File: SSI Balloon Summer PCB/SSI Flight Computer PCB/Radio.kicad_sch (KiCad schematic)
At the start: 5 parts, among them J3 LoRa antenna, U1 RFM95W-915S2

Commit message: Cleaned APRS Filter up and adding Testing points
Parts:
- added TP12, TP13, TP7: TestPoint, TestPoint:TestPoint_Pad_1.5x1.5mm, symbol Connector:TestPoint
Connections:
- net GND: now also TP13.1
- net LoRa_DIO0: now also TP12.1
- net LoRa_RESET: now also TP7.1

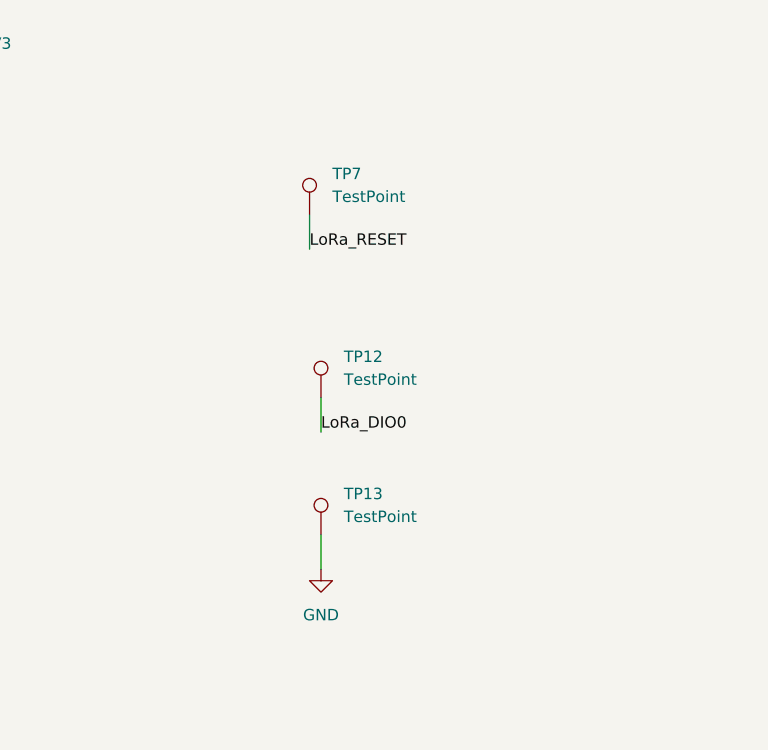
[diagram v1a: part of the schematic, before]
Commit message: Added Headers for testing, finalizing PCB
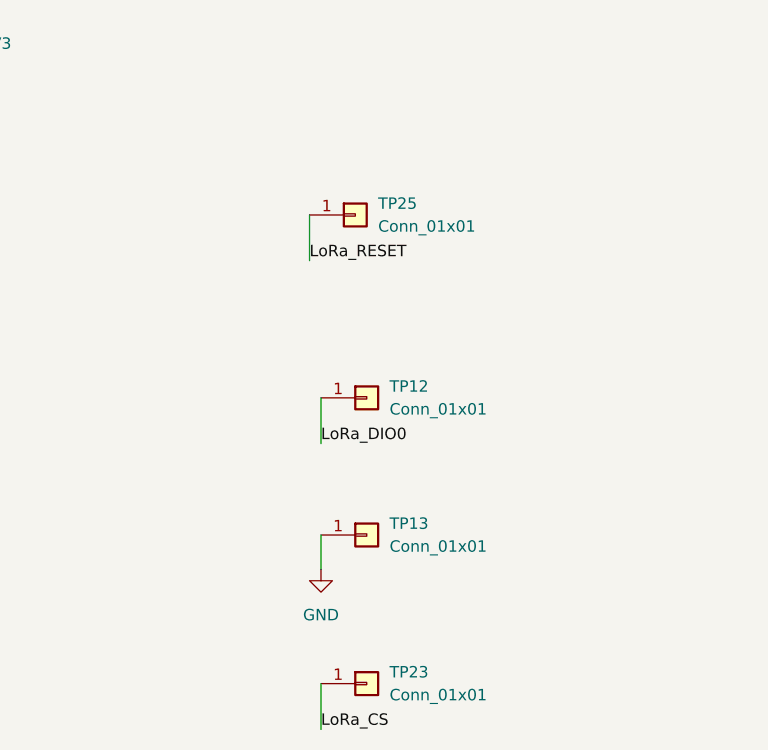
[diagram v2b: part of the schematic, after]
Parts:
- removed TP12, TP13, TP7: TestPoint, TestPoint:TestPoint_Pad_1.5x1.5mm, symbol Connector:TestPoint
- added TP12, TP13, TP23, TP25: Conn_01x01, Connector_PinHeader_2.54mm:PinHeader_1x01_P2.54mm_Vertical, symbol Connector_Generic:Conn_01x01
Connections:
- net GND: now also TP13.1 (Pin_1)
- net LoRa_CS: now also TP23.1 (Pin_1)
- net LoRa_DIO0: now also TP12.1 (Pin_1)
- net LoRa_RESET: now also TP25.1 (Pin_1)
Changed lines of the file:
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@@
+	(wire
+		(pts
+			(xy 231.14 139.7) (xy 231.14 144.78)
+		)
+		(stroke
+			(width 0)
+			(type default)
+		)
+	)
 	(wire
 		(pts
@@
 	(wire
 		(pts
-			(xy 229.87 87.63) (xy 229.87 91.44)
+			(xy 229.87 87.63) (xy 229.87 92.71)
 		)
 		(stroke
@@
 	(wire
 		(pts
-			(xy 231.14 107.95) (xy 231.14 111.76)
+			(xy 231.14 107.95) (xy 231.14 113.03)
 		)
 		(stroke
@@
 		)
 	)
+	(label "LoRa_CS"
+		(at 231.14 144.78 0)
+		(effects
+			(font
+				(size 1.27 1.27)
+			)
+			(justify left bottom)
+		)
+	)
 	(label "MISO"
 		(at 255.27 20.32 180)
@@
 	)
 	(label "LoRa_DIO0"
-		(at 231.14 111.76 0)
+		(at 231.14 113.03 0)
 		(effects
 			(font
@@
 	)
 	(label "LoRa_RESET"
-		(at 229.87 91.44 0)
+		(at 229.87 92.71 0)
 		(effects
 			(font
@@
 	)
 	(symbol
-		(lib_id "Connector:TestPoint")
-		(at 229.87 87.63 0)
+		(lib_id "Connector_Generic:Conn_01x01")
+		(at 236.22 123.19 0)
 		(unit 1)
 		(body_style 1)
@@
 		(dnp no)
 		(fields_autoplaced yes)
-		(property "Reference" "TP7"
-			(at 232.41 83.0579 0)
+		(property "Reference" "TP13"
+			(at 238.76 121.9199 0)
 			(show_name no)
 			(do_not_autoplace no)
@@
 			)
 		)
-		(property "Value" "TestPoint"
-			(at 232.41 85.5979 0)
+		(property "Value" "Conn_01x01"
+			(at 238.76 124.4599 0)
 			(show_name no)
 			(do_not_autoplace no)
@@
 			)
 		)
-		(property "Footprint" "TestPoint:TestPoint_Pad_1.5x1.5mm"
-			(at 234.95 87.63 0)
+		(property "Footprint" "Connector_PinHeader_2.54mm:PinHeader_1x01_P2.54mm_Vertical"
+			(at 236.22 123.19 0)
 			(hide yes)
 			(show_name no)
@@
 		)
 		(property "Datasheet" ""
-			(at 234.95 87.63 0)
-			(hide yes)
-			(show_name no)
-			(do_not_autoplace no)
-			(effects
-				(font
-					(size 1.27 1.27)
-				)
-			)
-		)
-		(property "Description" "test point"
-			(at 229.87 87.63 0)
-			(hide yes)
-			(show_name no)
-			(do_not_autoplace no)
-			(effects
-				(font
-					(size 1.27 1.27)
-				)
-			)
-		)
-		(property "PART_REV" ""
-			(at 229.87 87.63 0)
+			(at 236.22 123.19 0)
+			(hide yes)
+			(show_name no)
+			(do_not_autoplace no)
+			(effects
+				(font
+					(size 1.27 1.27)
+				)
+			)
+		)
+		(property "Description" "Generic connector, single row, 01x01, script generated (kicad-library-utils/schlib/autogen/connector/)"
+			(at 236.22 123.19 0)
 			(hide yes)
 			(show_name no)
@@
 			(project "SSI Summer Balloons"
 				(path "/3c45a535-6e6b-4825-ad52-82c10cbe7866/2467bfc8-9a58-45c6-9683-5b5ac73ee36d"
-					(reference "TP7")
+					(reference "TP13")
+					(unit 1)
+				)
+			)
+		)
+	)
+	(symbol
+		(lib_id "Connector_Generic:Conn_01x01")
+		(at 234.95 87.63 0)
+		(unit 1)
+		(body_style 1)
+		(exclude_from_sim no)
+		(in_bom yes)
+		(on_board yes)
+		(in_pos_files yes)
+		(dnp no)
+		(fields_autoplaced yes)
+		(property "Reference" "TP25"
+			(at 237.49 86.3599 0)
+			(show_name no)
+			(do_not_autoplace no)
+			(effects
+				(font
+					(size 1.27 1.27)
+				)
+				(justify left)
+			)
+		)
+		(property "Value" "Conn_01x01"
+			(at 237.49 88.8999 0)
+			(show_name no)
+			(do_not_autoplace no)
+			(effects
+				(font
+					(size 1.27 1.27)
+				)
+				(justify left)
+			)
+		)
+		(property "Footprint" "Connector_PinHeader_2.54mm:PinHeader_1x01_P2.54mm_Vertical"
+			(at 234.95 87.63 0)
+			(hide yes)
+			(show_name no)
+			(do_not_autoplace no)
+			(effects
+				(font
+					(size 1.27 1.27)
+				)
+			)
+		)
+		(property "Datasheet" ""
+			(at 234.95 87.63 0)
+			(hide yes)
+			(show_name no)
+			(do_not_autoplace no)
+			(effects
+				(font
+					(size 1.27 1.27)
+				)
+			)
+		)
+		(property "Description" "Generic connector, single row, 01x01, script generated (kicad-library-utils/schlib/autogen/connector/)"
+			(at 234.95 87.63 0)
+			(hide yes)
+			(show_name no)
+			(do_not_autoplace no)
+			(effects
+				(font
+					(size 1.27 1.27)
+				)
+			)
+		)
+		(pin "1"
+		)
+		(instances
+			(project "SSI Summer Balloons"
+				(path "/3c45a535-6e6b-4825-ad52-82c10cbe7866/2467bfc8-9a58-45c6-9683-5b5ac73ee36d"
+					(reference "TP25")
 					(unit 1)
 				)
@@
 				(path "/3c45a535-6e6b-4825-ad52-82c10cbe7866/2467bfc8-9a58-45c6-9683-5b5ac73ee36d"
 					(reference "R6")
-					(unit 1)
-				)
-			)
-		)
-	)
-	(symbol
-		(lib_id "Connector:TestPoint")
-		(at 231.14 107.95 0)
-		(unit 1)
-		(body_style 1)
-		(exclude_from_sim no)
-		(in_bom yes)
-		(on_board yes)
-		(in_pos_files yes)
-		(dnp no)
-		(fields_autoplaced yes)
-		(property "Reference" "TP12"
-			(at 233.68 103.3779 0)
-			(show_name no)
-			(do_not_autoplace no)
-			(effects
-				(font
-					(size 1.27 1.27)
-				)
-				(justify left)
-			)
-		)
-		(property "Value" "TestPoint"
-			(at 233.68 105.9179 0)
-			(show_name no)
-			(do_not_autoplace no)
-			(effects
-				(font
-					(size 1.27 1.27)
-				)
-				(justify left)
-			)
-		)
-		(property "Footprint" "TestPoint:TestPoint_Pad_1.5x1.5mm"
-			(at 236.22 107.95 0)
-			(hide yes)
-			(show_name no)
-			(do_not_autoplace no)
-			(effects
-				(font
-					(size 1.27 1.27)
-				)
-			)
-		)
-		(property "Datasheet" ""
-			(at 236.22 107.95 0)
-			(hide yes)
-			(show_name no)
-			(do_not_autoplace no)
-			(effects
-				(font
-					(size 1.27 1.27)
-				)
-			)
-		)
-		(property "Description" "test point"
-			(at 231.14 107.95 0)
-			(hide yes)
-			(show_name no)
-			(do_not_autoplace no)
-			(effects
-				(font
-					(size 1.27 1.27)
-				)
-			)
-		)
-		(property "PART_REV" ""
-			(at 231.14 107.95 0)
-			(hide yes)
-			(show_name no)
-			(do_not_autoplace no)
-			(effects
-				(font
-					(size 1.27 1.27)
-				)
-			)
-		)
-		(pin "1"
-		)
-		(instances
-			(project "SSI Summer Balloons"
-				(path "/3c45a535-6e6b-4825-ad52-82c10cbe7866/2467bfc8-9a58-45c6-9683-5b5ac73ee36d"
-					(reference "TP12")
 					(unit 1)
 				)
@@
 	)
 	(symbol
-		(lib_id "Connector:TestPoint")
-		(at 231.14 123.19 0)
+		(lib_id "Connector_Generic:Conn_01x01")
+		(at 236.22 107.95 0)
 		(unit 1)
 		(body_style 1)
@@
 		(dnp no)
 		(fields_autoplaced yes)
-		(property "Reference" "TP13"
-			(at 233.68 118.6179 0)
+		(property "Reference" "TP12"
+			(at 238.76 106.6799 0)
 			(show_name no)
 			(do_not_autoplace no)
@@
 			)
 		)
-		(property "Value" "TestPoint"
-			(at 233.68 121.1579 0)
+		(property "Value" "Conn_01x01"
+			(at 238.76 109.2199 0)
 			(show_name no)
 			(do_not_autoplace no)
@@
 			)
 		)
-		(property "Footprint" "TestPoint:TestPoint_Pad_1.5x1.5mm"
-			(at 236.22 123.19 0)
+		(property "Footprint" "Connector_PinHeader_2.54mm:PinHeader_1x01_P2.54mm_Vertical"
+			(at 236.22 107.95 0)
 			(hide yes)
 			(show_name no)
@@
 		)
 		(property "Datasheet" ""
-			(at 236.22 123.19 0)
-			(hide yes)
-			(show_name no)
-			(do_not_autoplace no)
-			(effects
-				(font
-					(size 1.27 1.27)
-				)
-			)
-		)
-		(property "Description" "test point"
-			(at 231.14 123.19 0)
-			(hide yes)
-			(show_name no)
-			(do_not_autoplace no)
-			(effects
-				(font
-					(size 1.27 1.27)
-				)
-			)
-		)
-		(property "PART_REV" ""
-			(at 231.14 123.19 0)
+			(at 236.22 107.95 0)
+			(hide yes)
+			(show_name no)
+			(do_not_autoplace no)
+			(effects
+				(font
+					(size 1.27 1.27)
+				)
+			)
+		)
+		(property "Description" "Generic connector, single row, 01x01, script generated (kicad-library-utils/schlib/autogen/connector/)"
+			(at 236.22 107.95 0)
 			(hide yes)
 			(show_name no)
@@
 			(project "SSI Summer Balloons"
 				(path "/3c45a535-6e6b-4825-ad52-82c10cbe7866/2467bfc8-9a58-45c6-9683-5b5ac73ee36d"
-					(reference "TP13")
+					(reference "TP12")
 					(unit 1)
 				)
+			)
+		)
+	)
+	(symbol
+		(lib_id "Connector_Generic:Conn_01x01")
+		(at 236.22 139.7 0)
+		(unit 1)
+		(body_style 1)
+		(exclude_from_sim no)
+		(in_bom yes)
+		(on_board yes)
+		(in_pos_files yes)
+		(dnp no)
+		(fields_autoplaced yes)
+		(property "Reference" "TP23"
+			(at 238.76 138.4299 0)
+			(show_name no)
+			(do_not_autoplace no)
+			(effects
+				(font
+					(size 1.27 1.27)
+				)
+				(justify left)
+			)
+		)
+		(property "Value" "Conn_01x01"
+			(at 238.76 140.9699 0)
+			(show_name no)
+			(do_not_autoplace no)
+			(effects
+				(font
+					(size 1.27 1.27)
+				)
+				(justify left)
+			)
+		)
+		(property "Footprint" "Connector_PinHeader_2.54mm:PinHeader_1x01_P2.54mm_Vertical"
+			(at 236.22 139.7 0)
+			(hide yes)
+			(show_name no)
+			(do_not_autoplace no)
+			(effects
+				(font
+					(size 1.27 1.27)
+				)
+			)
+		)
+		(property "Datasheet" ""
+			(at 236.22 139.7 0)
+			(hide yes)
+			(show_name no)
+			(do_not_autoplace no)
+			(effects
+				(font
+					(size 1.27 1.27)
+				)
+			)
+		)
+		(property "Description" "Generic connector, single row, 01x01, script generated (kicad-library-utils/schlib/autogen/connector/)"
+			(at 236.22 139.7 0)
+			(hide yes)
+			(show_name no)
+			(do_not_autoplace no)
+			(effects
+				(font
+					(size 1.27 1.27)
+				)
+			)
+		)
+		(pin "1"
+		)
+		(instances
+			(project "SSI Summer Balloons"
+				(path "/3c45a535-6e6b-4825-ad52-82c10cbe7866/2467bfc8-9a58-45c6-9683-5b5ac73ee36d"
+					(reference "TP23")
+					(unit 1)
+				)

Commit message: More silkscreen organization, combined some pinheaders
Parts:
- TP12: value Conn_01x01 -> LoRa_DIO0
- TP13: value Conn_01x01 -> GND
- TP23: value Conn_01x01 -> LoRa_CS
- TP25: value Conn_01x01 -> LoRa_RESET
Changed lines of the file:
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@@
 			)
 		)
-		(property "Value" "Conn_01x01"
+		(property "Value" "GND"
 			(at 238.76 124.4599 0)
 			(show_name no)
@@
 			)
 		)
-		(property "Value" "Conn_01x01"
+		(property "Value" "LoRa_RESET"
 			(at 237.49 88.8999 0)
 			(show_name no)
@@
 			)
 		)
-		(property "Value" "Conn_01x01"
+		(property "Value" "LoRa_DIO0"
 			(at 238.76 109.2199 0)
 			(show_name no)
@@
 			)
 		)
-		(property "Value" "Conn_01x01"
+		(property "Value" "LoRa_CS"
 			(at 238.76 140.9699 0)
 			(show_name no)

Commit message: Updated antenna connector
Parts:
- J3: footprint Connector_Coaxial:U.FL_Hirose_U.FL-R-SMT-1_Vertical -> Connector_Coaxial:SMA_Amphenol_901-144_Vertical
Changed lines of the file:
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@@
 			)
 		)
-		(property "Footprint" "Connector_Coaxial:U.FL_Hirose_U.FL-R-SMT-1_Vertical"
+		(property "Footprint" "Connector_Coaxial:SMA_Amphenol_901-144_Vertical"
 			(at 107.95 91.44 0)
 			(hide yes)

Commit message: finished finding all parts on JLCPCB - finalizing BOM then order
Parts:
- C13: LCSC (none) -> C519438
- C14: LCSC (none) -> C5189822
- J3: LCSC (none) -> C376663
- R6: LCSC (none) -> C25804
- TP12, TP13, TP23, TP25: LCSC (none) -> C81276
- U1: LCSC (none) -> C2844473
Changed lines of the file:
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@@
+			)
+		)
+		(property "LCSC" "C5189822"
+			(at 181.61 67.31 0)
+			(hide yes)
+			(show_name no)
+			(do_not_autoplace no)
+			(effects
+				(font
+					(size 1.27 1.27)
+				)
 			)
 		)
@@
 			)
 		)
-		(property "Datasheet" ""
+		(property "Datasheet" "HAND SOLDER THIS"
 			(at 107.95 91.44 0)
 			(hide yes)
@@
 		)
 		(property "PART_REV" ""
+			(at 107.95 91.44 0)
+			(hide yes)
+			(show_name no)
+			(do_not_autoplace no)
+			(effects
+				(font
+					(size 1.27 1.27)
+				)
+			)
+		)
+		(property "LCSC" "C376663"
 			(at 107.95 91.44 0)
 			(hide yes)
@@
 			)
 		)
-		(property "Datasheet" ""
+		(property "Datasheet" "slightly dif module"
 			(at 151.13 93.98 0)
 			(hide yes)
@@
 		)
 		(property "PART_REV" ""
+			(at 151.13 93.98 0)
+			(hide yes)
+			(show_name no)
+			(do_not_autoplace no)
+			(effects
+				(font
+					(size 1.27 1.27)
+				)
+			)
+		)
+		(property "LCSC" "C2844473"
 			(at 151.13 93.98 0)
 			(hide yes)
@@
 			)
 		)
-		(property "Datasheet" ""
+		(property "Datasheet" "C81276"
 			(at 236.22 123.19 0)
 			(hide yes)
@@
 		)
 		(property "Description" "Generic connector, single row, 01x01, script generated (kicad-library-utils/schlib/autogen/connector/)"
+			(at 236.22 123.19 0)
+			(hide yes)
+			(show_name no)
+			(do_not_autoplace no)
+			(effects
+				(font
+					(size 1.27 1.27)
+				)
+			)
+		)
+		(property "LCSC" "C81276"
 			(at 236.22 123.19 0)
 			(hide yes)
@@
 			)
 		)
-		(property "Datasheet" ""
+		(property "Datasheet" "C81276"
 			(at 234.95 87.63 0)
 			(hide yes)
@@
 		)
 		(property "Description" "Generic connector, single row, 01x01, script generated (kicad-library-utils/schlib/autogen/connector/)"
+			(at 234.95 87.63 0)
+			(hide yes)
+			(show_name no)
+			(do_not_autoplace no)
+			(effects
+				(font
+					(size 1.27 1.27)
+				)
+			)
+		)
+		(property "LCSC" "C81276"
 			(at 234.95 87.63 0)
 			(hide yes)
@@
 		)
 		(property "PART_REV" ""
+			(at 120.65 78.74 0)
+			(hide yes)
+			(show_name no)
+			(do_not_autoplace no)
+			(effects
+				(font
+					(size 1.27 1.27)
+				)
+			)
+		)
+		(property "LCSC" "C25804"
 			(at 120.65 78.74 0)
 			(hide yes)
@@
 			)
 		)
-		(property "Datasheet" ""
+		(property "Datasheet" "C81276"
 			(at 236.22 107.95 0)
 			(hide yes)
@@
 		)
 		(property "Description" "Generic connector, single row, 01x01, script generated (kicad-library-utils/schlib/autogen/connector/)"
+			(at 236.22 107.95 0)
+			(hide yes)
+			(show_name no)
+			(do_not_autoplace no)
+			(effects
+				(font
+					(size 1.27 1.27)
+				)
+			)
+		)
+		(property "LCSC" "C81276"
 			(at 236.22 107.95 0)
 			(hide yes)
@@
 			)
 		)
-		(property "Datasheet" ""
+		(property "Datasheet" "C81276"
 			(at 236.22 139.7 0)
 			(hide yes)
@@
 		)
 		(property "Description" "Generic connector, single row, 01x01, script generated (kicad-library-utils/schlib/autogen/connector/)"
+			(at 236.22 139.7 0)
+			(hide yes)
+			(show_name no)
+			(do_not_autoplace no)
+			(effects
+				(font
+					(size 1.27 1.27)
+				)
+			)
+		)
+		(property "LCSC" "C81276"
 			(at 236.22 139.7 0)
 			(hide yes)
@@
 			(at 171.45 67.31 0)
 			(hide yes)
+			(show_name no)
+			(do_not_autoplace no)
+			(effects
+				(font
+					(size 1.27 1.27)
+				)
+			)
+		)
+		(property "LCSC" "C519438"
+			(at 171.45 67.31 0)
+			(hide yes)

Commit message: PCB finally done i think and ready to order
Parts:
- C13: LCSC C519438 -> C14663
- C14: LCSC C5189822 -> C15850
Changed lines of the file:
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@@
 			)
 		)
-		(property "LCSC" "C5189822"
+		(property "LCSC" "C15850"
 			(at 181.61 67.31 0)
 			(hide yes)
@@
 			)
 		)
-		(property "LCSC" "C519438"
+		(property "LCSC" "C14663"
 			(at 171.45 67.31 0)
 			(hide yes)

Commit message: Board done but we have a price crisis so might have to change things
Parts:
- J3, TP12, TP13, TP23, TP25: now not fitted; now left out of the parts list
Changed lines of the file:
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@@
 		(body_style 1)
 		(exclude_from_sim no)
-		(in_bom yes)
+		(in_bom no)
 		(on_board yes)
 		(in_pos_files yes)
-		(dnp no)
+		(dnp yes)
 		(fields_autoplaced yes)
 		(property "Reference" "J3"
@@
 		(body_style 1)
 		(exclude_from_sim no)
-		(in_bom yes)
+		(in_bom no)
 		(on_board yes)
 		(in_pos_files yes)
-		(dnp no)
+		(dnp yes)
 		(fields_autoplaced yes)
 		(property "Reference" "TP13"
@@
 		(body_style 1)
 		(exclude_from_sim no)
-		(in_bom yes)
+		(in_bom no)
 		(on_board yes)
 		(in_pos_files yes)
-		(dnp no)
+		(dnp yes)
 		(fields_autoplaced yes)
 		(property "Reference" "TP25"
@@
 		(body_style 1)
 		(exclude_from_sim no)
-		(in_bom yes)
+		(in_bom no)
 		(on_board yes)
 		(in_pos_files yes)
-		(dnp no)
+		(dnp yes)
 		(fields_autoplaced yes)
 		(property "Reference" "TP12"
@@
 		(body_style 1)
 		(exclude_from_sim no)
-		(in_bom yes)
+		(in_bom no)
 		(on_board yes)
 		(in_pos_files yes)
-		(dnp no)
+		(dnp yes)
 		(fields_autoplaced yes)
 		(property "Reference" "TP23"
